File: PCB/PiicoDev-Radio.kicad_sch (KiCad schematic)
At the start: 32 parts, among them J1 , J2 , J3 Conn_01x05_Male, SW1 ADDR, U1 ATtiny1616-M, U2 RFM69HCW

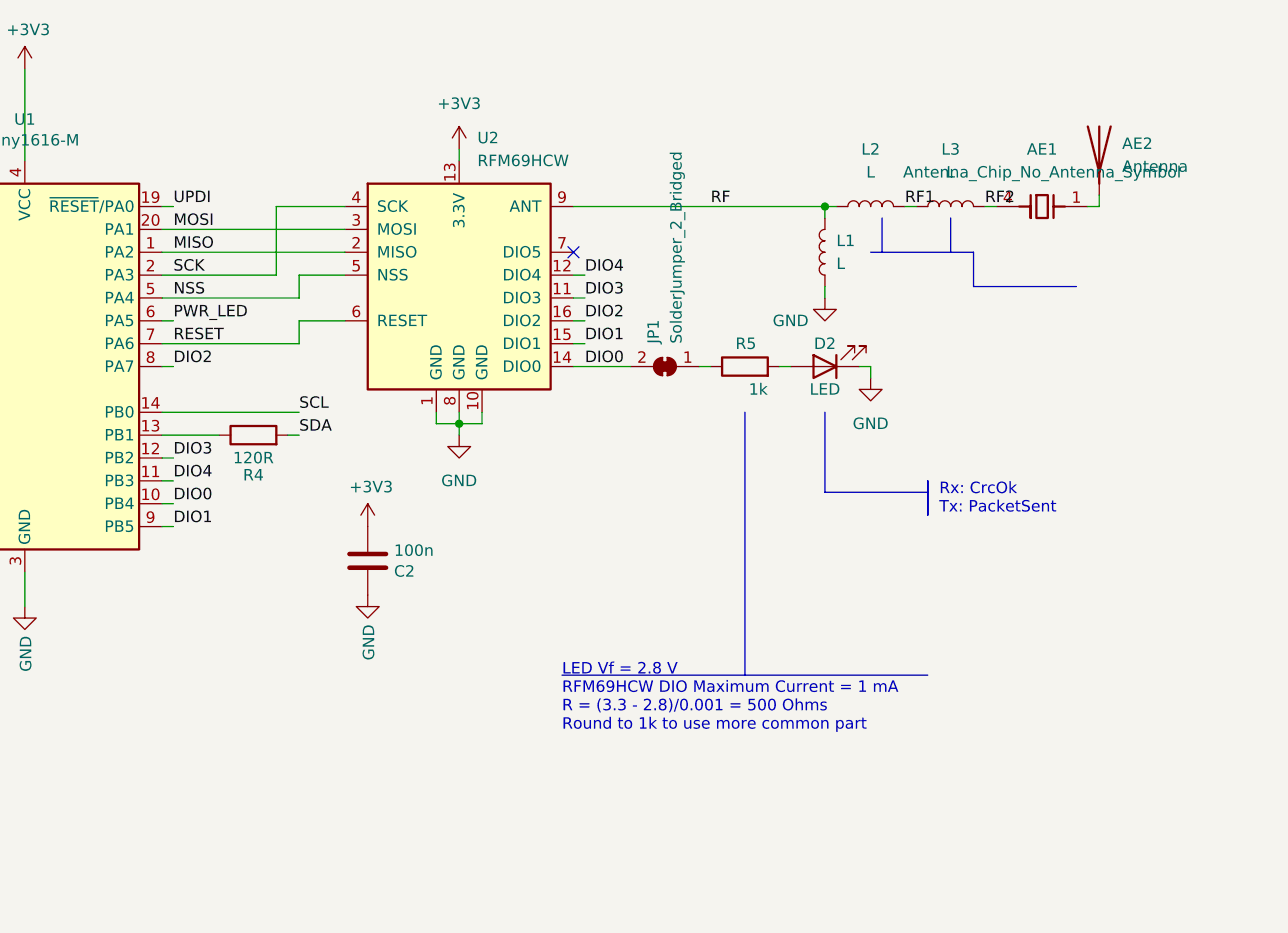
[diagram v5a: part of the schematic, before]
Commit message: v10 Improve RFM69HCW footprint
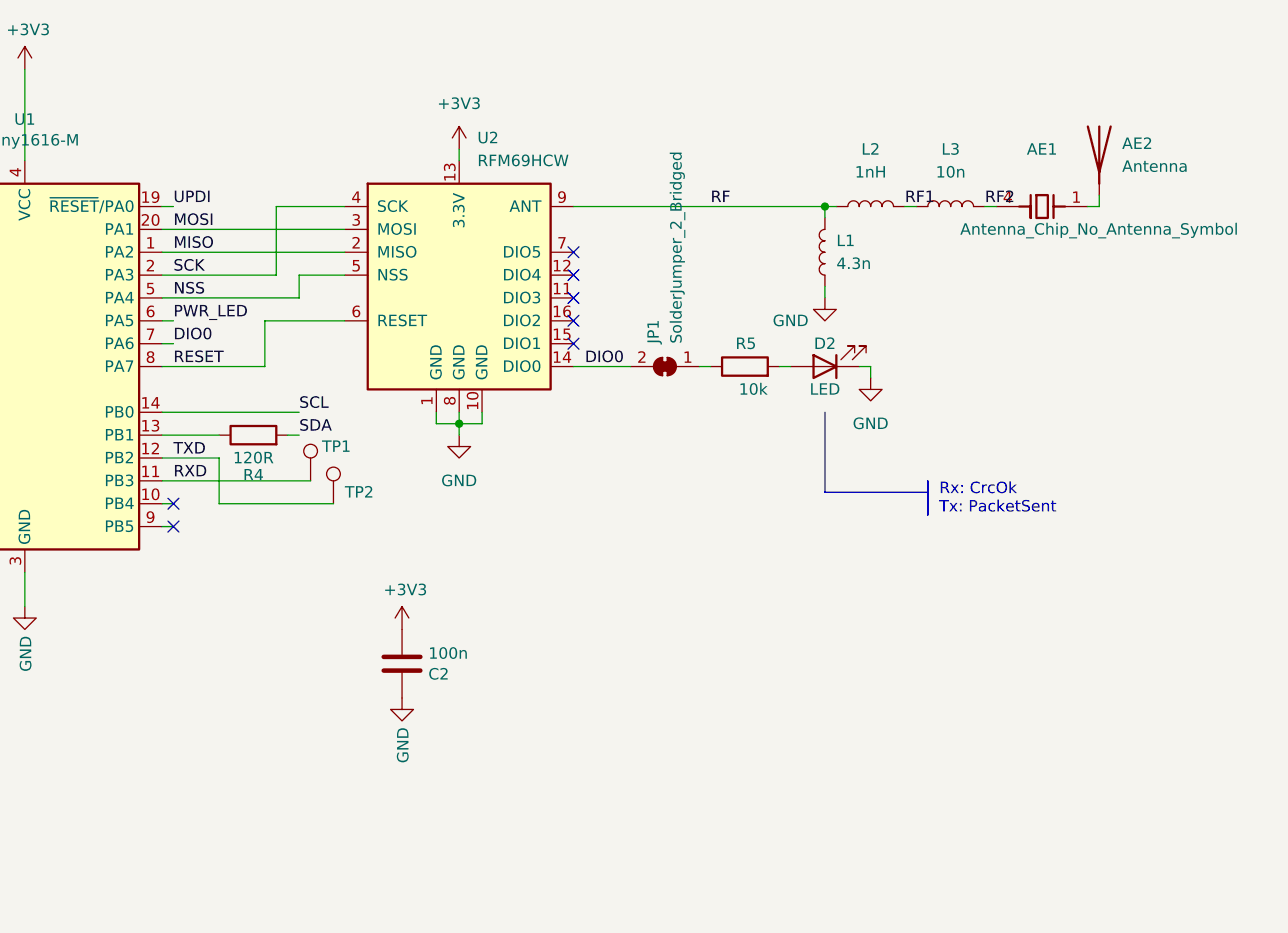
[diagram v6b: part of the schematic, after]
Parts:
- added TP1, TP2: TestPoint, TestPoint:TestPoint_Pad_1.5x1.5mm, symbol Connector:TestPoint
- L1: value L -> 4.3n
- L2: value L -> 1nH
- L3: value L -> 10n
- R5: value 1k -> 10k
- U2: footprint RF_Module:HOPERF_RFM9XW_SMD -> CoreElectronics_Components:HOPERF_RFM69HCW_SMD
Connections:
- net DIO0: now also U1.7 (PA6); no longer U1.10 (PB4)
- net RESET: now also U1.8 (PA7); no longer U1.7 (PA6)
- net DIO1: no longer names the net of U1.9 (PB5)
- net DIO1: no longer U2.15 (DIO1)
- net DIO2: no longer names the net of U2.16 (DIO2)
- net DIO2: no longer U1.8 (PA7)
- net DIO3: no longer names the net of U2.11 (DIO3)
- net DIO3: no longer U1.12 (PB2)
- net DIO4: no longer names the net of U2.12 (DIO4)
- net DIO4: no longer U1.11 (PB3)
- new net RXD: TP1.1, U1.11 (PB3)
- new net TXD: TP2.1, U1.12 (PB2)
- no-connect marks 1 -> 7
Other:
- note removed: "LED Vf = 2.8 V RFM69HCW DIO Maximum Current = 1 mA R = (3.3 - 2.8)/0.001 = 500 Ohms Round to 1k to use more common part"
- moved on the sheet: C2
